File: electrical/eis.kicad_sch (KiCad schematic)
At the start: 39 parts

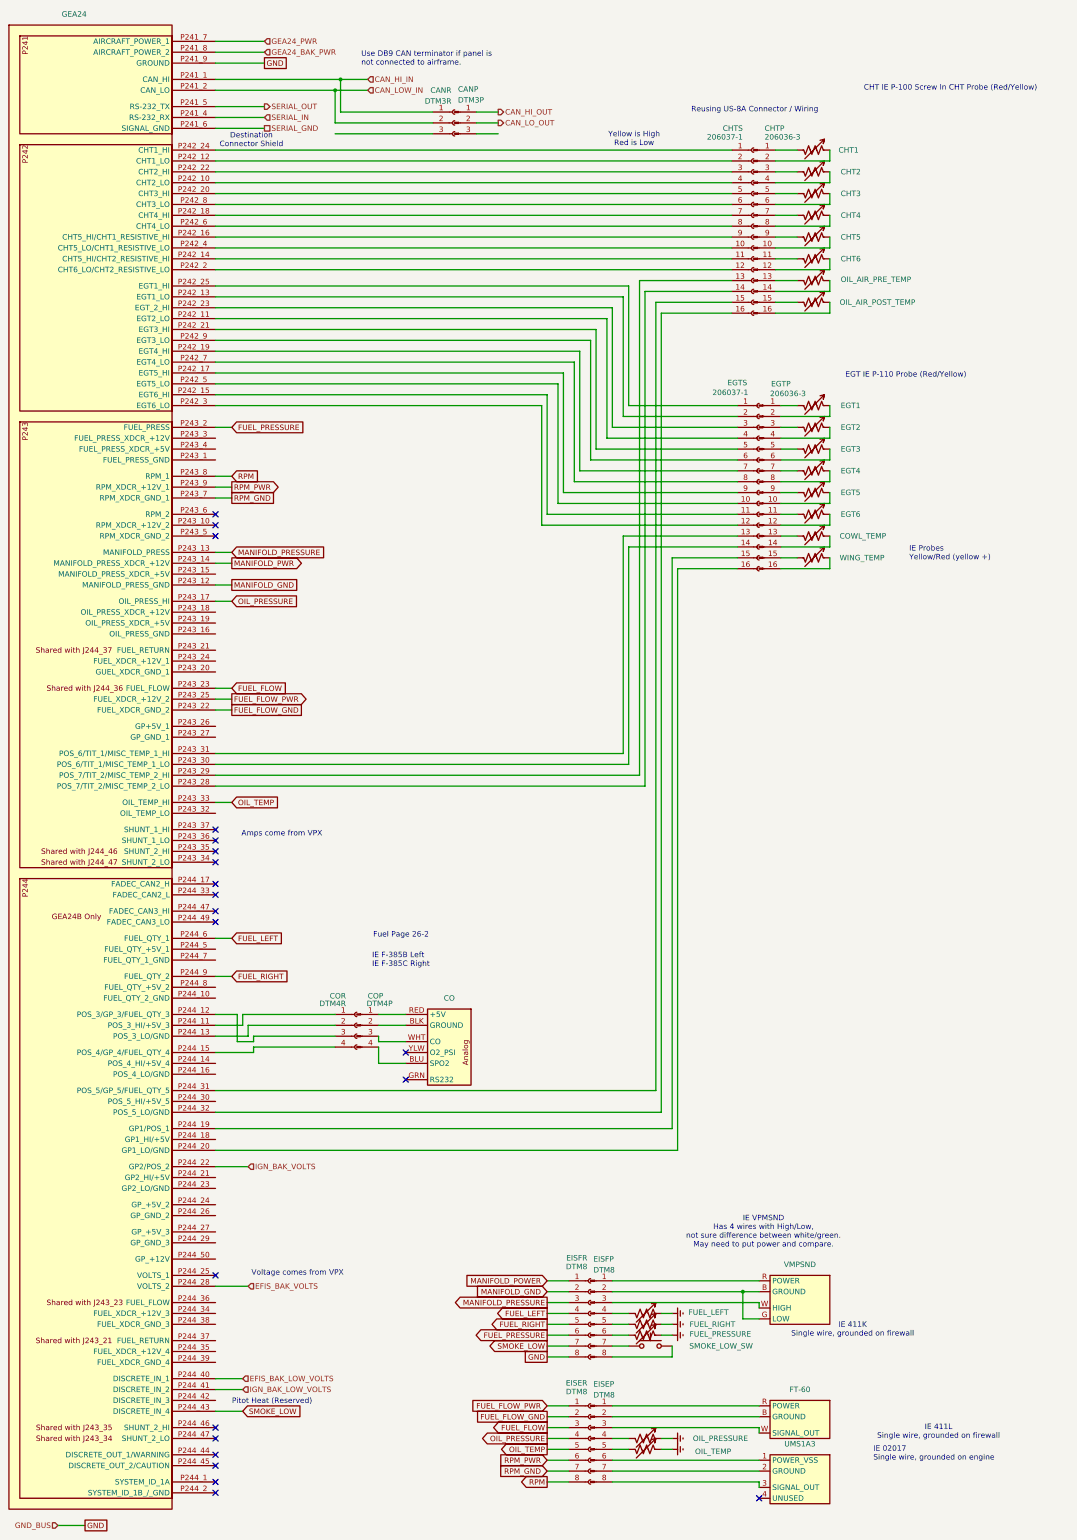
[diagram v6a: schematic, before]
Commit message: Changed to use Garmin sensors and their own connectors.
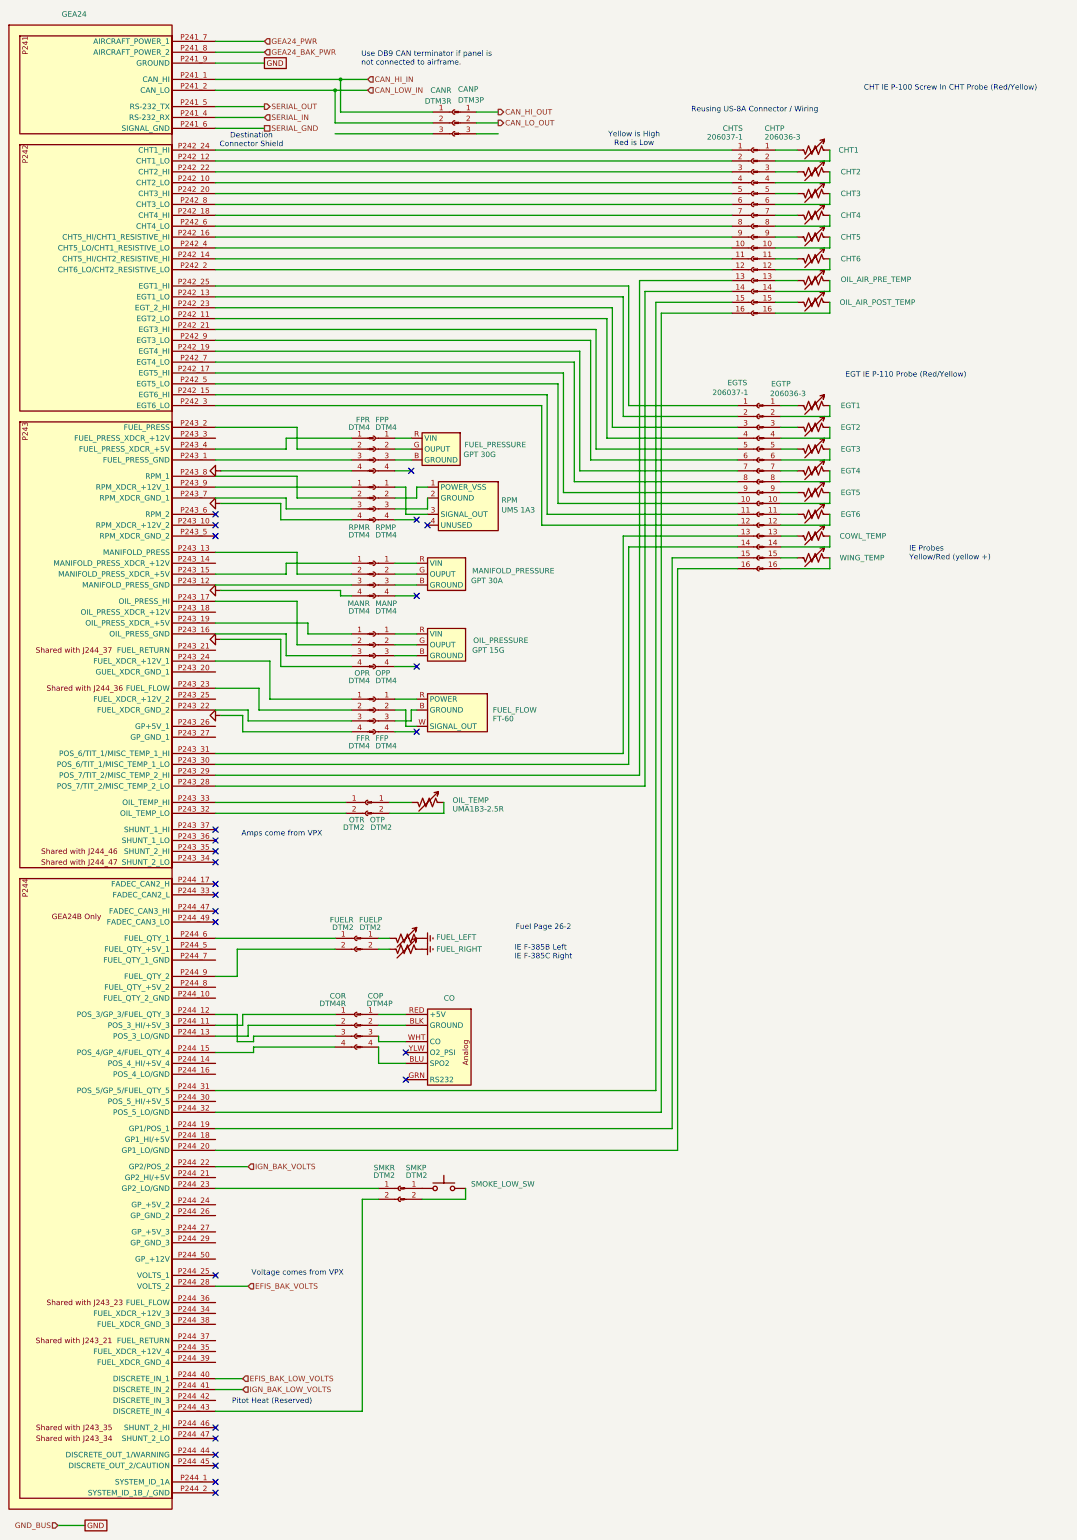
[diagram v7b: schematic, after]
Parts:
- removed EISEP, EISFP: DTM8, symbol Connector:Conn_01x08_Pin
- removed EISER, EISFR: DTM8, symbol Connector:Conn_01x08_Socket
- removed FUEL_PRESSURE, OIL_PRESSURE: R_Variable_US, symbol Device:R_Variable_US
- removed VMPSND: ~, symbol flyerx:IE_VMPSND
- added FFP, FPP, MANP, OPP, RPMP: DTM4, symbol Connector:Conn_01x04_Socket
- added FFR, FPR, MANR, OPR, RPMR: DTM4, symbol Connector:Conn_01x04_Pin
- added FUELP, OTP, SMKP: DTM2, symbol Connector:Conn_01x02_Pin
- added FUELR, OTR, SMKR: DTM2, symbol Connector:Conn_01x02_Socket
- added FUEL_PRESSURE: GPT 30G, symbol flyerx:Garmin_Sensor
- added MANIFOLD_PRESSURE: GPT 30A, symbol flyerx:Garmin_Sensor
- added OIL_PRESSURE: GPT 15G, symbol flyerx:Garmin_Sensor
- FUEL_FLOW: renamed from FT-60; value ~ -> FT-60
- OIL_TEMP: value R_Variable_US -> UMA1B3-2.5R
- RPM: renamed from UMS1A3; value ~ -> UMS 1A3
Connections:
- net Earth: no longer OIL_TEMP.1
- net at FUEL_FLOW.B (GROUND): now also FFP.3 (Pin_3)
- net at FUEL_FLOW.R (POWER): now also FFP.1 (Pin_1)
- net at FUEL_FLOW.W (SIGNAL_OUT): now also FFP.2 (Pin_2)
- net at GEA24.P243_1 (FUEL_PRESS_GND): now also FPR.3 (Pin_3)
- net at GEA24.P243_15 (MANIFOLD_PRESS_XDCR_+5V): now also MANR.1 (Pin_1)
- net at GEA24.P243_16 (OIL_PRESS_GND): now also OPR.3 (Pin_3)
- net at GEA24.P243_19 (OIL_PRESS_XDCR_+5V): now also OPR.1 (Pin_1)
- net at GEA24.P243_24 (FUEL_XDCR_+12V_1): now also FFR.1 (Pin_1)
- net at GEA24.P243_32 (OIL_TEMP_LO): now also OTR.2 (Pin_2)
- net at GEA24.P243_4 (FUEL_PRESS_XDCR_+5V): now also FPR.1 (Pin_1)
- net at GEA24.P244_23 (GP2_LO/GND): now also SMKR.1 (Pin_1)
- net at FUEL_LEFT.2: now also FUELP.1 (Pin_1)
- net at FUEL_RIGHT.2: now also FUELP.2 (Pin_2)
- net at RPM.1 (POWER_VSS): now also RPMP.2 (Pin_2)
- net at RPM.2 (GROUND): now also RPMP.3 (Pin_3)
- net at RPM.3 (SIGNAL_OUT): now also RPMP.1 (Pin_1)
- net at SMOKE_LOW_SW.1: now also SMKP.1 (Pin_1)
- net at SMOKE_LOW_SW.2: now also SMKP.2 (Pin_2)
- net at OIL_TEMP.2: now also OTP.1 (Pin_1)
- net FUEL_FLOW: no longer names the net of GEA24.P243_23 (FUEL_FLOW)
- net FUEL_FLOW: now also FFR.2 (Pin_2)
- net FUEL_FLOW_GND: no longer names the net of GEA24.P243_22 (FUEL_XDCR_GND_2)
- net FUEL_FLOW_GND: now also FFR.3 (Pin_3)
- net FUEL_FLOW_PWR: no longer names the net of GEA24.P243_25 (FUEL_XDCR_+12V_2)
- net FUEL_LEFT: no longer names the net of GEA24.P244_6 (FUEL_QTY_1)
- net FUEL_LEFT: now also FUELR.1 (Pin_1)
- net FUEL_PRESSURE: no longer names the net of GEA24.P243_2 (FUEL_PRESS)
- net FUEL_PRESSURE: now also FPR.2 (Pin_2)
- net FUEL_RIGHT: no longer names the net of GEA24.P244_9 (FUEL_QTY_2)
- net FUEL_RIGHT: now also FUELR.2 (Pin_2)
- net MANIFOLD_GND: no longer names the net of GEA24.P243_12 (MANIFOLD_PRESS_GND)
- net MANIFOLD_GND: now also MANR.3 (Pin_3)
- net MANIFOLD_PRESSURE: no longer names the net of GEA24.P243_13 (MANIFOLD_PRESS)
- net MANIFOLD_PRESSURE: now also MANR.2 (Pin_2)
- net MANIFOLD_PWR: no longer names the net of GEA24.P243_14 (MANIFOLD_PRESS_XDCR_+12V)
- net OIL_PRESSURE: no longer names the net of GEA24.P243_17 (OIL_PRESS_HI)
- net OIL_PRESSURE: now also OPR.2 (Pin_2)
- net OIL_TEMP: no longer names the net of GEA24.P243_33 (OIL_TEMP_HI)
- net OIL_TEMP: now also OTR.1 (Pin_1)
- net RPM: no longer names the net of GEA24.P243_8 (RPM_1)
- net RPM: now also RPMR.2 (Pin_2)
- net RPM_GND: no longer names the net of GEA24.P243_7 (RPM_XDCR_GND_1)
- net RPM_GND: now also RPMR.3 (Pin_3)
- net RPM_PWR: no longer names the net of GEA24.P243_9 (RPM_XDCR_+12V_1)
- net RPM_PWR: now also RPMR.1 (Pin_1)
- net SMOKE_LOW: no longer names the net of GEA24.P244_43 (DISCRETE_IN_4)
- net SMOKE_LOW: now also SMKR.2 (Pin_2)
- new net: MANIFOLD_PRESSURE.B (GROUND), MANP.3 (Pin_3)
- new net: MANIFOLD_PRESSURE.G (OUPUT), MANP.2 (Pin_2)
- new net: MANIFOLD_PRESSURE.R (VIN), MANP.1 (Pin_1)
- new net: FPP.1 (Pin_1), FUEL_PRESSURE.R (VIN)
- new net: FPP.2 (Pin_2), FUEL_PRESSURE.G (OUPUT)
- new net: FPP.3 (Pin_3), FUEL_PRESSURE.B (GROUND)
- new net: OIL_TEMP.1, OTP.2 (Pin_2)
- new net: OIL_PRESSURE.R (VIN), OPP.1 (Pin_1)
- new net: OIL_PRESSURE.G (OUPUT), OPP.2 (Pin_2)
- new net: OIL_PRESSURE.B (GROUND), OPP.3 (Pin_3)
- new net GNDS: FFR.4 (Pin_4), FPR.4 (Pin_4), MANR.4 (Pin_4), OPR.4 (Pin_4), RPMR.4 (Pin_4)
- no-connect marks 21 -> 26
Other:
- note removed: "IE 02017 Single wire, grounded on engine"
- note removed: "IE 411K Single wire, grounded on firewall"
- note removed: "IE 411L Single wire, grounded on firewall"
- note removed: "IE VPMSND Has 4 wires with High/Low, not sure difference between white/green. May need to put power and compare."
- moved on the sheet: FUEL_FLOW, FUEL_LEFT, FUEL_RIGHT, OIL_TEMP, RPM, SMOKE_LOW_SW
